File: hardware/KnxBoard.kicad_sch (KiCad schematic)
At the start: 9 parts, among them J1 Conn_01x16, J2 Conn_01x16, J3 Conn_01x12, J4 Conn_01x02_Male

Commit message: Progress
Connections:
- net KNXIFACE/KNX_V3.3 renamed KNXIFACE/+3.3V
- net MCU/MCU_V33 renamed MCU/VDD
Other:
- sheet KNXIFACE ports: added +12V, +3.3V, GNDREF; removed KNX_GND, KNX_V12, KNX_V3.3
- sheet MCU ports: added GNDREF, VDD; removed MCU_GND, MCU_V33
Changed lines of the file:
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@@
     (pin "2")
+  )
+  (symbol (lib_id "power:VDD") (at 218.44 46.99 90) (unit 1)
+    (in_bom yes) (on_board yes) (fields_autoplaced)
+    (property "Reference" "#PWR0109" (id 0) (at 222.25 46.99 0)
+      (effects (font (size 1.27 1.27)) hide)
+    )
+    (property "Value" "VDD" (id 1) (at 214.63 46.9899 90)
+      (effects (font (size 1.27 1.27)) (justify left))
+    )
+    (property "Footprint" "" (id 2) (at 218.44 46.99 0)
+      (effects (font (size 1.27 1.27)) hide)
+    )
+    (property "Datasheet" "" (id 3) (at 218.44 46.99 0)
+      (effects (font (size 1.27 1.27)) hide)
+    )
+    (pin "1")
   )
   (symbol (lib_id "power:+12V") (at 77.47 68.58 270) (unit 1)
@@
     )
     (property "Datasheet" "" (id 3) (at 218.44 151.13 0)
-      (effects (font (size 1.27 1.27)) hide)
-    )
-    (pin "1")
-  )
-  (symbol (lib_id "power:VDD") (at 218.44 153.67 90) (unit 1)
-    (in_bom yes) (on_board yes)
-    (property "Reference" "#PWR0113" (id 0) (at 222.25 153.67 0)
-      (effects (font (size 1.27 1.27)) hide)
-    )
-    (property "Value" "VDD" (id 1) (at 213.36 153.67 90))
-    (property "Footprint" "" (id 2) (at 218.44 153.67 0)
-      (effects (font (size 1.27 1.27)) hide)
-    )
-    (property "Datasheet" "" (id 3) (at 218.44 153.67 0)
       (effects (font (size 1.27 1.27)) hide)
     )
@@
     )
     (property "Datasheet" "" (id 3) (at 218.44 41.91 0)
+      (effects (font (size 1.27 1.27)) hide)
+    )
+    (pin "1")
+  )
+  (symbol (lib_id "power:VDD") (at 218.44 153.67 90) (unit 1)
+    (in_bom yes) (on_board yes) (fields_autoplaced)
+    (property "Reference" "#PWR0105" (id 0) (at 222.25 153.67 0)
+      (effects (font (size 1.27 1.27)) hide)
+    )
+    (property "Value" "VDD" (id 1) (at 214.63 153.6699 90)
+      (effects (font (size 1.27 1.27)) (justify left))
+    )
+    (property "Footprint" "" (id 2) (at 218.44 153.67 0)
+      (effects (font (size 1.27 1.27)) hide)
+    )
+    (property "Datasheet" "" (id 3) (at 218.44 153.67 0)
+      (effects (font (size 1.27 1.27)) hide)
+    )
+    (pin "1")
+  )
+  (symbol (lib_id "power:VDD") (at 218.44 83.82 90) (unit 1)
+    (in_bom yes) (on_board yes) (fields_autoplaced)
+    (property "Reference" "#PWR0108" (id 0) (at 222.25 83.82 0)
+      (effects (font (size 1.27 1.27)) hide)
+    )
+    (property "Value" "VDD" (id 1) (at 214.63 83.8199 90)
+      (effects (font (size 1.27 1.27)) (justify left))
+    )
+    (property "Footprint" "" (id 2) (at 218.44 83.82 0)
+      (effects (font (size 1.27 1.27)) hide)
+    )
+    (property "Datasheet" "" (id 3) (at 218.44 83.82 0)
       (effects (font (size 1.27 1.27)) hide)
     )
@@
     (pin "9")
   )
-  (symbol (lib_id "power:VDD") (at 218.44 46.99 90) (unit 1)
-    (in_bom yes) (on_board yes)
-    (property "Reference" "#PWR0108" (id 0) (at 222.25 46.99 0)
-      (effects (font (size 1.27 1.27)) hide)
-    )
-    (property "Value" "VDD" (id 1) (at 213.36 46.99 90))
-    (property "Footprint" "" (id 2) (at 218.44 46.99 0)
-      (effects (font (size 1.27 1.27)) hide)
-    )
-    (property "Datasheet" "" (id 3) (at 218.44 46.99 0)
-      (effects (font (size 1.27 1.27)) hide)
-    )
-    (pin "1")
-  )
   (symbol (lib_id "Jumper:SolderJumper_2_Open") (at 107.95 74.93 180) (unit 1)
     (in_bom yes) (on_board yes) (fields_autoplaced)
@@
     (pin "1")
     (pin "2")
-  )
-  (symbol (lib_id "power:VDD") (at 218.44 83.82 90) (unit 1)
-    (in_bom yes) (on_board yes)
-    (property "Reference" "#PWR0105" (id 0) (at 222.25 83.82 0)
-      (effects (font (size 1.27 1.27)) hide)
-    )
-    (property "Value" "VDD" (id 1) (at 213.36 83.82 90))
-    (property "Footprint" "" (id 2) (at 218.44 83.82 0)
-      (effects (font (size 1.27 1.27)) hide)
-    )
-    (property "Datasheet" "" (id 3) (at 218.44 83.82 0)
-      (effects (font (size 1.27 1.27)) hide)
-    )
-    (pin "1")
   )
   (symbol (lib_id "Connector_Generic:Conn_01x16") (at 223.52 133.35 0) (unit 1)
@@
       (effects (font (size 1.27 1.27)) (justify right))
     )
-    (pin "KNX_GND" output (at 77.47 101.6 0)
-      (effects (font (size 1.27 1.27)) (justify right))
-    )
-    (pin "KNX_V3.3" output (at 77.47 74.93 0)
-      (effects (font (size 1.27 1.27)) (justify right))
-    )
     (pin "KNX+" input (at 41.91 83.82 180)
       (effects (font (size 1.27 1.27)) (justify left))
@@
       (effects (font (size 1.27 1.27)) (justify left))
     )
-    (pin "KNX_V12" output (at 77.47 68.58 0)
-      (effects (font (size 1.27 1.27)) (justify right))
-    )
     (pin "RESETB" output (at 77.47 96.52 0)
       (effects (font (size 1.27 1.27)) (justify right))
@@
     )
     (pin "CLK16MHZ" output (at 77.47 88.9 0)
+      (effects (font (size 1.27 1.27)) (justify right))
+    )
+    (pin "+12V" output (at 77.47 68.58 0)
+      (effects (font (size 1.27 1.27)) (justify right))
+    )
+    (pin "+3.3V" output (at 77.47 74.93 0)
+      (effects (font (size 1.27 1.27)) (justify right))
+    )
+    (pin "GNDREF" output (at 77.47 101.6 0)
       (effects (font (size 1.27 1.27)) (justify right))
     )
@@
       (effects (font (size 1.27 1.27)) (justify left))
     )
-    (pin "MCU_GND" input (at 153.67 101.6 180)
-      (effects (font (size 1.27 1.27)) (justify left))
-    )
-    (pin "MCU_V33" input (at 153.67 74.93 180)
-      (effects (font (size 1.27 1.27)) (justify left))
-    )
     (pin "PB13" bidirectional (at 196.85 146.05 0)
       (effects (font (size 1.27 1.27)) (justify right))
@@
     (pin "PH1" bidirectional (at 196.85 88.9 0)
       (effects (font (size 1.27 1.27)) (justify right))
+    )
+    (pin "GNDREF" input (at 153.67 101.6 180)
+      (effects (font (size 1.27 1.27)) (justify left))
+    )
+    (pin "VDD" input (at 153.67 74.93 180)
+      (effects (font (size 1.27 1.27)) (justify left))
     )
   )
@@
       (reference "#PWR0104") (unit 1) (value "GNDREF") (footprint "")
     )
-    (path "/f3fc4559-d7f0-4587-986c-afbacda02cd2"
+    (path "/63d06dee-333a-4cda-b96e-d9753592e109"
       (reference "#PWR0105") (unit 1) (value "VDD") (footprint "")
     )
@@
       (reference "#PWR0107") (unit 1) (value "GNDREF") (footprint "")
     )
-    (path "/b4d1a9ff-7029-4d88-bd2d-2dc1a62ddefb"
+    (path "/6b02f891-3897-4eda-bf52-9781beb451b1"
       (reference "#PWR0108") (unit 1) (value "VDD") (footprint "")
     )
-    (path "/d8441614-dec4-4bc1-b184-c502a3d79ed5/942768fa-d357-4ac8-8c40-f037d6648e04"
+    (path "/1f28e666-08ca-4533-a0f9-b8ef0cf3a34a"
       (reference "#PWR0109") (unit 1) (value "VDD") (footprint "")
     )
@@
       (reference "#PWR0111") (unit 1) (value "GNDREF") (footprint "")
     )
-    (path "/d8441614-dec4-4bc1-b184-c502a3d79ed5/ac8178a7-da6d-4f88-97b2-e0db79482ec1"
+    (path "/d8441614-dec4-4bc1-b184-c502a3d79ed5/f7806dcd-71e9-4123-92b7-ea99280c7f64"
       (reference "#PWR0112") (unit 1) (value "VDD") (footprint "")
     )
-    (path "/59037098-9a35-43ca-a94a-65dd555019db"
+    (path "/d8441614-dec4-4bc1-b184-c502a3d79ed5/f6ee3763-9f63-4d66-8c6a-8e8ae5884c34"
       (reference "#PWR0113") (unit 1) (value "VDD") (footprint "")
     )
@@
       (reference "#PWR0123") (unit 1) (value "GNDREF") (footprint "")
     )
-    (path "/60177bd8-6562-4452-843e-ff6a093b4415/77ebf47f-e1d0-4519-8199-d5158efcd707"
-      (reference "#PWR0124") (unit 1) (value "GND") (footprint "")
+    (path "/60177bd8-6562-4452-843e-ff6a093b4415/71746e08-0b26-48d0-bd1c-2499c9203f7e"
+      (reference "#PWR0124") (unit 1) (value "GNDREF") (footprint "")
     )
     (path "/60177bd8-6562-4452-843e-ff6a093b4415/6eb22094-8b3e-49f0-8989-2e622c12a153"
@@
       (reference "#PWR0129") (unit 1) (value "+3.3V") (footprint "")
     )
-    (path "/60177bd8-6562-4452-843e-ff6a093b4415/48de7eec-6807-4ec7-bc65-58700888663d"
-      (reference "#PWR0130") (unit 1) (value "GND") (footprint "")
-    )
-    (path "/60177bd8-6562-4452-843e-ff6a093b4415/645a3b21-7a52-496d-83f4-8477c88fdeac"
-      (reference "#PWR0131") (unit 1) (value "GND") (footprint "")
+    (path "/60177bd8-6562-4452-843e-ff6a093b4415/f956d0e5-1697-46f2-a21a-1c5f1425614c"
+      (reference "#PWR0131") (unit 1) (value "GNDREF") (footprint "")
     )
     (path "/60177bd8-6562-4452-843e-ff6a093b4415/d5bc4329-3ca5-44ec-89dc-0ac10bdf6950"
       (reference "#PWR0132") (unit 1) (value "+3.3V") (footprint "")
     )
+    (path "/60177bd8-6562-4452-843e-ff6a093b4415/6eecba6d-b1ad-43df-ba6f-6b5ef9051bc4"
+      (reference "#PWR0133") (unit 1) (value "GNDREF") (footprint "")
+    )
+    (path "/60177bd8-6562-4452-843e-ff6a093b4415/983da9d3-9aeb-4ce2-aad5-1fea20d29489"
+      (reference "#PWR?") (unit 1) (value "GNDREF") (footprint "")
+    )
     (path "/082dec17-2d5d-4dc3-aea8-299af407049c"

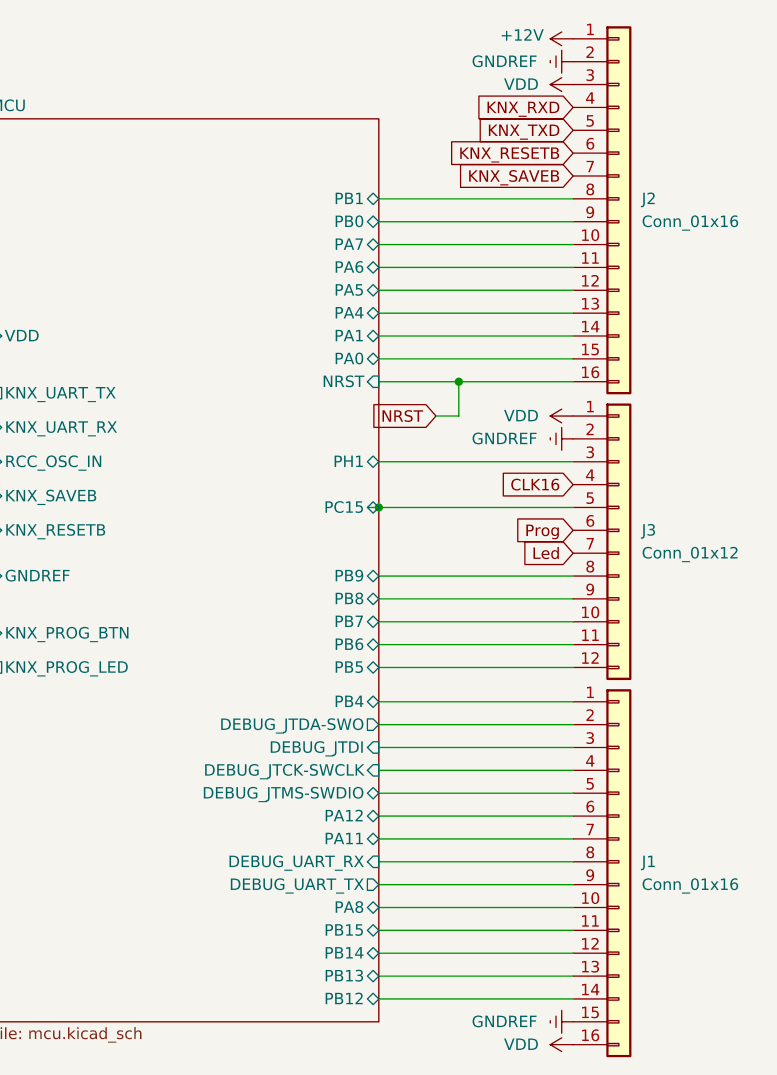
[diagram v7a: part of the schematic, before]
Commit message: Switch to STM32G491KEU6 with NCN5130
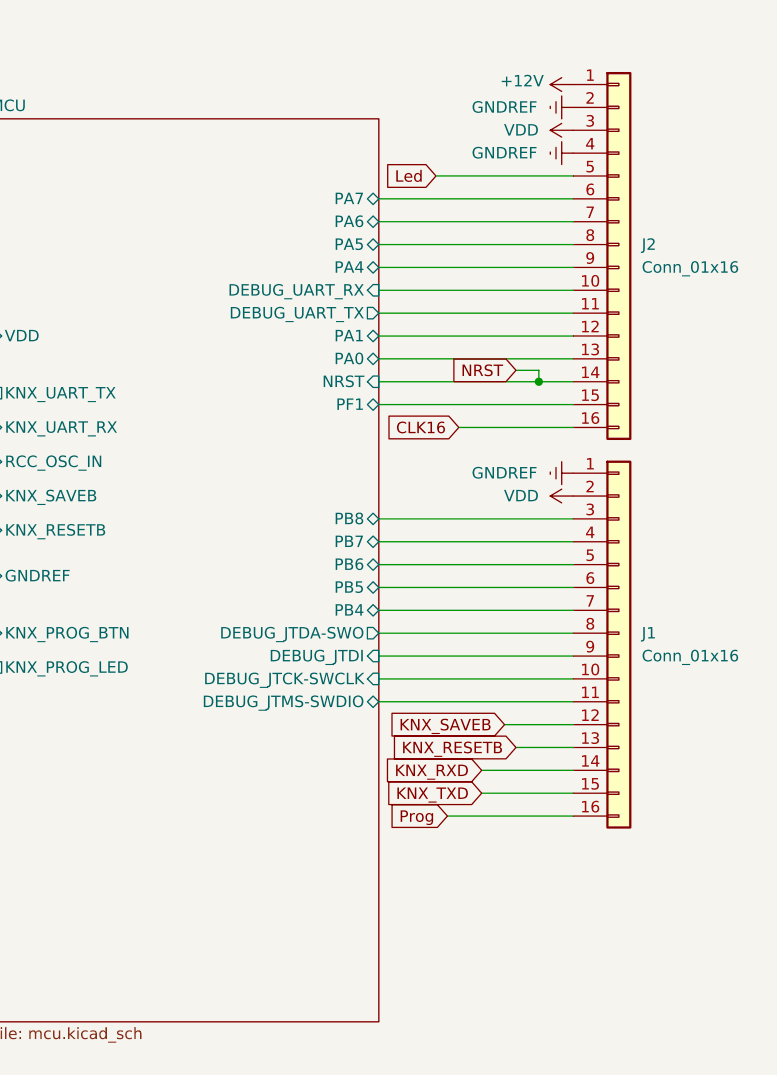
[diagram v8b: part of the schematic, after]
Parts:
- removed J3: Conn_01x12, Connector_PinHeader_2.54mm:PinHeader_1x12_P2.54mm_Vertical, symbol Connector_Generic:Conn_01x12
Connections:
- net MCU/PA11 is gone; now on net MCU/PB4: J1.7 (Pin_7)
- net MCU/PA12 is gone; now on net MCU/PB5: J1.6 (Pin_6)
- net MCU/PA8 is gone; now on net MCU/DEBUG_JTCK-SWCLK: J1.10 (Pin_10)
- net MCU/PB0 is gone; now on net MCU/PA4: J2.9 (Pin_9)
- net MCU/PB1 is gone; now on net MCU/PA5: J2.8 (Pin_8)
- net MCU/PB12 is gone; now on net KNX_RXD: J1.14 (Pin_14)
- net MCU/PB13 is gone; now on net KNX_RESETB: J1.13 (Pin_13)
- net MCU/PB14 is gone; now on net KNX_SAVEB: J1.12 (Pin_12)
- net MCU/PB15 is gone; now on net MCU/DEBUG_JTMS-SWDIO: J1.11 (Pin_11)
- net CLK16: now also J2.16 (Pin_16)
- net GNDREF: now also J1.1 (Pin_1), J2.4 (Pin_4); no longer J1.15 (Pin_15)
- net KNX_RESETB: no longer J2.6 (Pin_6)
- net KNX_RXD: no longer J2.4 (Pin_4)
- net KNX_SAVEB: no longer J2.7 (Pin_7)
- net KNX_TXD: now also J1.15 (Pin_15); no longer J2.5 (Pin_5)
- net Led: now also J2.5 (Pin_5)
- net MCU/DEBUG_JTCK-SWCLK: no longer J1.4 (Pin_4)
- net MCU/DEBUG_JTDA-SWO: now also J1.8 (Pin_8); no longer J1.2 (Pin_2)
- net MCU/DEBUG_JTDI: now also J1.9 (Pin_9); no longer J1.3 (Pin_3)
- net MCU/DEBUG_JTMS-SWDIO: no longer J1.5 (Pin_5)
- net MCU/DEBUG_UART_RX: now also J2.10 (Pin_10); no longer J1.8 (Pin_8)
- net MCU/DEBUG_UART_TX: now also J2.11 (Pin_11); no longer J1.9 (Pin_9)
- net MCU/PA0: now also J2.13 (Pin_13); no longer J2.15 (Pin_15)
- net MCU/PA1: now also J2.12 (Pin_12); no longer J2.14 (Pin_14)
- net MCU/PA4: no longer J2.13 (Pin_13)
- net MCU/PA5: no longer J2.12 (Pin_12)
- net MCU/PA6: now also J2.7 (Pin_7); no longer J2.11 (Pin_11)
- net MCU/PA7: now also J2.6 (Pin_6); no longer J2.10 (Pin_10)
- net MCU/PB4: no longer J1.1 (Pin_1)
- net MCU/PB6: now also J1.5 (Pin_5)
- net MCU/PB7: now also J1.4 (Pin_4)
- net MCU/PB8: now also J1.3 (Pin_3)
- net NRST: now also J2.14 (Pin_14); no longer J2.16 (Pin_16)
- net Prog: now also J1.16 (Pin_16)
- net VDD: now also J1.2 (Pin_2); no longer J1.16 (Pin_16)
- new net MCU/PF1: J2.15 (Pin_15)
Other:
- sheet MCU ports: added PF1; removed PA11, PA12, PA8, PB0, PB1, PB12, PB13, PB14, PB15, PB9, PC15, PH1
- moved on the sheet: J1, J2
